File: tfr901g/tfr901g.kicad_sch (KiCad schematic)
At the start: 35 parts, among them J1 Conn_01x08, J2 Conn_01x08, J3 Conn_01x08, J4 Conn_01x08, J5 Conn_01x08, J6 Conn_01x08, J7 Conn_01x08, J8 Conn_01x08, J9 Conn_01x08, P1 Power Bus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

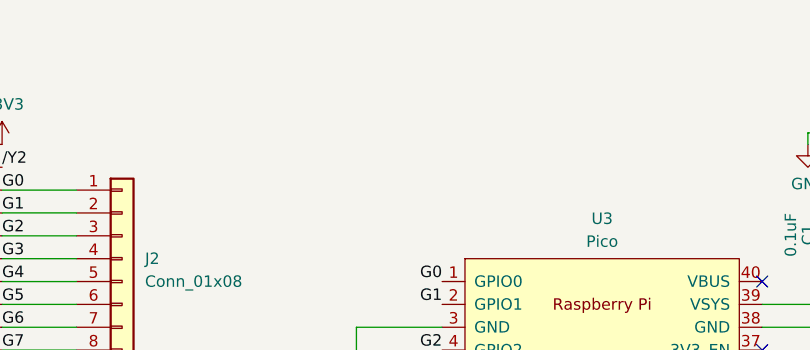
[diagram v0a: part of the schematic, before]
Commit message: add python firmware
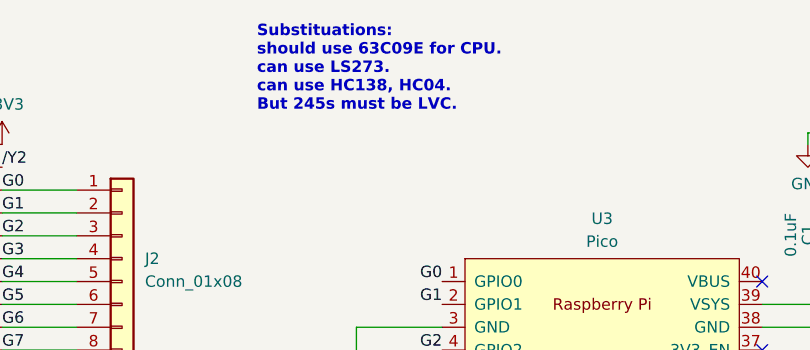
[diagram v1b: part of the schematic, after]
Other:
- note added: "Substituations: should use 63C09E for CPU. can use LS273. can use HC138, HC04. But 245s must be LVC."
